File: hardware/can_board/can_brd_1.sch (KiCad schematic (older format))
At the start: 11 parts, among them P471 CONN_4, P472 CONN_2, U471 SN65HVD230

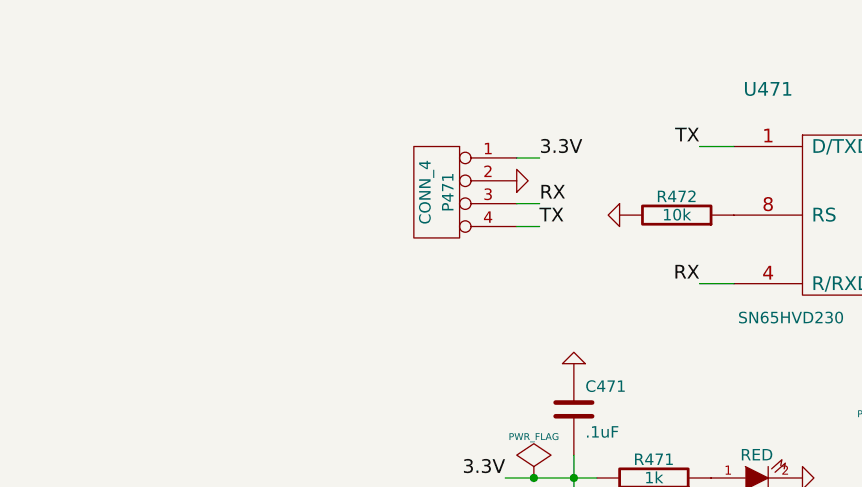
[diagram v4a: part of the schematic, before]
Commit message: better net names
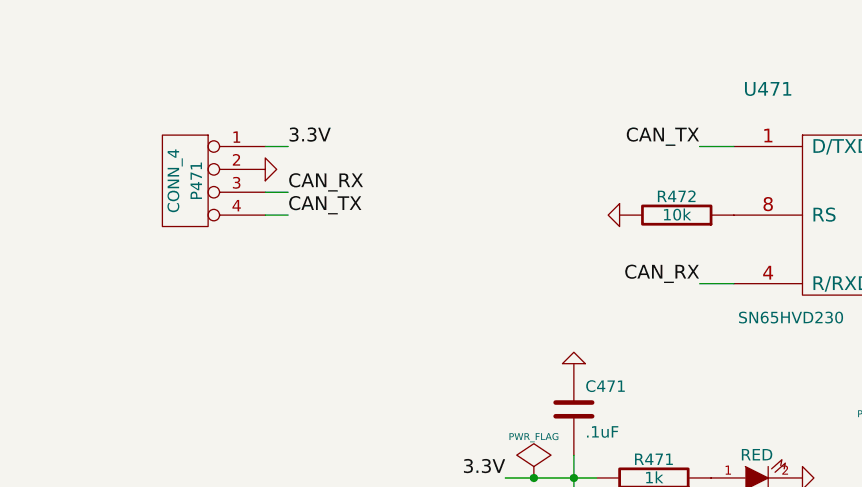
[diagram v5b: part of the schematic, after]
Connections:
- net RX renamed CAN_RX
- net TX renamed CAN_TX
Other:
- moved on the sheet: P471
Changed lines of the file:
@@
 LIBS:logo_flipped
 LIBS:can_brd_1-cache
-EELAYER 24 0
+EELAYER 27 0
 EELAYER END
 $Descr A4 11693 8268
@@
 Sheet 1 1
 Title ""
-Date "08 Янв 2014"
+Date "19 jan 2014"
 Rev ""
 Comp ""
@@
 L CONN_4 P471
 U 1 1 52CADBD0
-P 2950 1750
-F 0 "P471" V 2900 1750 50  0000 C CNN
-F 1 "CONN_4" V 3000 1750 50  0000 C CNN
-F 2 "" H 2950 1750 60  0000 C CNN
-F 3 "" H 2950 1750 60  0000 C CNN
-	1    2950 1750
+P 1850 1700
+F 0 "P471" V 1800 1700 50  0000 C CNN
+F 1 "CONN_4" V 1900 1700 50  0000 C CNN
+F 2 "" H 1850 1700 60  0000 C CNN
+F 3 "" H 1850 1700 60  0000 C CNN
+	1    1850 1700
 	-1   0    0    -1
 $EndComp
-Text Label 3400 1600 0    60   ~ 0
+Text Label 2300 1550 0    60   ~ 0
 3.3V
 $Comp
 L GND #PWR07
 U 1 1 52CADB3B
-P 3300 1700
-F 0 "#PWR07" H 3300 1700 30  0001 C CNN
-F 1 "GND" H 3300 1630 30  0001 C CNN
-F 2 "" H 3300 1700 60  0001 C CNN
-F 3 "" H 3300 1700 60  0001 C CNN
-	1    3300 1700
+P 2200 1650
+F 0 "#PWR07" H 2200 1650 30  0001 C CNN
+F 1 "GND" H 2200 1580 30  0001 C CNN
+F 2 "" H 2200 1650 60  0001 C CNN
+F 3 "" H 2200 1650 60  0001 C CNN
+	1    2200 1650
 	0    -1   -1   0
 $EndComp
-Text Label 3400 1800 0    60   ~ 0
-RX
-Text Label 3400 1900 0    60   ~ 0
-TX
+Text Label 2300 1750 0    60   ~ 0
+CAN_RX
+Text Label 2300 1850 0    60   ~ 0
+CAN_TX
 Text Label 4100 1550 2    60   ~ 0
-TX
+CAN_TX
 Text Label 4100 2150 2    60   ~ 0
-RX
+CAN_RX
 Connection ~ -4675 3450
 Wire Wire Line
@@
 Connection ~ 3375 3000
 Wire Wire Line
-	3300 1800 3400 1800
-Wire Wire Line
-	3300 1900 3400 1900
-Wire Wire Line
-	3300 1600 3400 1600
+	2200 1750 2300 1750
+Wire Wire Line
+	2200 1850 2300 1850
+Wire Wire Line
+	2200 1550 2300 1550
 Wire Wire Line
 	4250 2150 4100 2150
